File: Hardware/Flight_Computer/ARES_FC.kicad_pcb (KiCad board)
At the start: 2 copper layers, 57.2 x 57.2 mm, 63 parts, among them J1 SWD, J2 TYPE-C-31-M-12, J3 FC_M/P, J4 5V, J5 GND, J6 FC_RF, U1 STM32F401CCU6, U2 AMS1117-3.3, U3 BMP280, U4 BNO055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

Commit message: added tentative external i2c connectors
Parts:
- added J7: Conn_01x04_Pin, Connector_JST:JST_SH_BM04B-SRSS-TB_1x04-1MP_P1.00mm_Vertical, F.Cu at (147.2, 63.1)
- added J8: Conn_01x04_Pin, Connector_JST:JST_SH_BM04B-SRSS-TB_1x04-1MP_P1.00mm_Vertical, F.Cu at (161.3, 63.2)

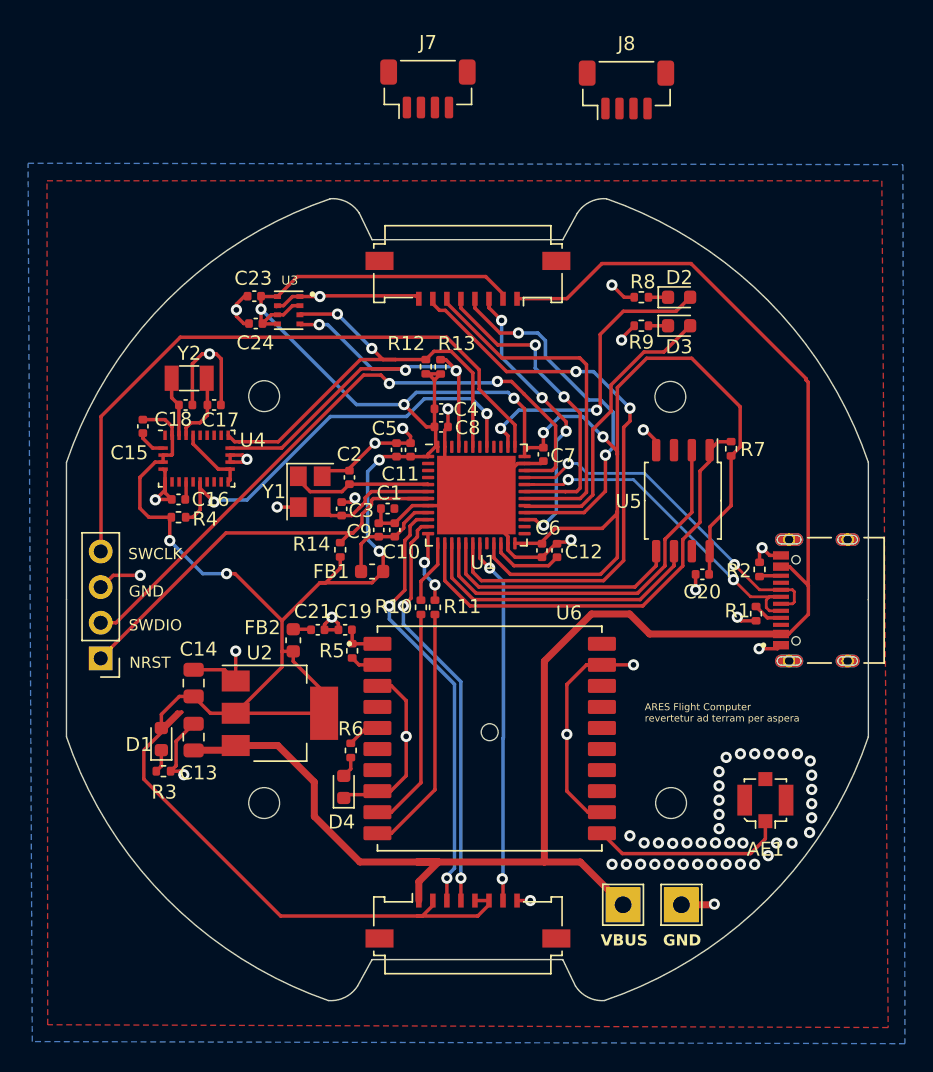
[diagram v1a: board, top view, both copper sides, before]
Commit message: fixed motor conn. i2c and external i2c conn.s, changed PNs, added models
new PN for Y2, added 3D models for BMP, Antenna, and ext. i2c connectors.
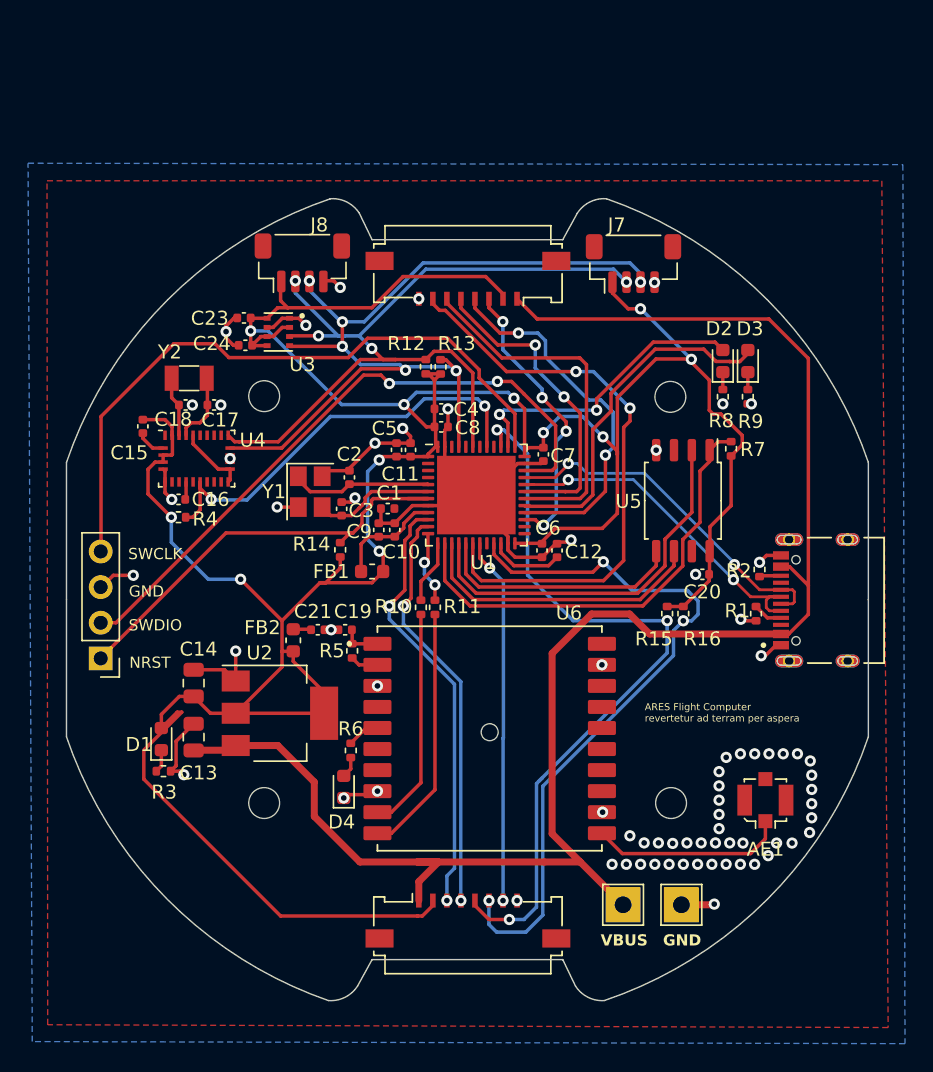
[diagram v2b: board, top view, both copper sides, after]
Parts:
- added R15: 4.7k, Resistor_SMD:R_0402_1005Metric, F.Cu at (164.2, 100.5)
- added R16: 4.7k, Resistor_SMD:R_0402_1005Metric, F.Cu at (165.3, 100.5)
- Y2: value 32.768Mhz -> 32.768kHz
- moved J8 26.2 mm to (138.2, 75.5)
- moved J7 19.2 mm to (161.8, 75.5)
- moved R8 9.16 mm to (168.2, 85.0), turned to -90 degrees
- moved R9 9.12 mm to (169.9, 85.0), turned to -90 degrees
- moved D2 5.52 mm to (168.2, 82.5), turned to 90 degrees
- moved D3 5.51 mm to (169.9, 82.5), turned to 90 degrees
- moved C23 1.72 mm to (134.0, 79.4)
- moved C24 1.72 mm to (134.1, 81.4)
- moved U3 1.72 mm to (136.5, 80.4)
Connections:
- J3 pad 5: +3.3V -> /MOTOR_SDA
- J3 pad 6: +3.3V -> /MOTOR_SCL
- U1 pad 21: +3.3V -> /MOTOR_SCL
- U1 pad 39: +3.3V -> /MOTOR_SDA
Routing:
- net GND: track 137.0 -> 82.3 mm, vias 67 -> 73
- net /MOTOR_SDA: track 0.00 -> 54.3 mm, vias 0 -> 3
- net /MOTOR_SCL: track 0.00 -> 51.0 mm, vias 0 -> 3
- net /SCL: track 34.6 -> 64.8 mm, vias 3 -> 6
- net /SDA: track 34.4 -> 62.0 mm, vias 2 -> 4
- net +3.3V: track 242.7 -> 236.1 mm, vias 9 -> 11
- net /LED_B: track 21.0 -> 25.0 mm
- net /SWCLK: track 46.4 -> 47.2 mm
- net /LED_G: track 21.9 -> 21.3 mm
- net VBUS: track 122.5 -> 122.0 mm

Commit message: added BOMs
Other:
- board text added: "TO MOTOR/POWER BOARD"
- board text added: "TO RF BOARD"
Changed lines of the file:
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@@
 			(outputformat 1)
 			(mirror no)
-			(drillshape 1)
+			(drillshape 0)
 			(scaleselection 1)
-			(outputdirectory "")
+			(outputdirectory "manufacturing/gbr/")
 		)
 	)
@@
 		)
 	)
+	(gr_text "TO RF BOARD"
+		(at 147.25 79.95 0)
+		(layer "F.SilkS")
+		(effects
+			(font
+				(size 0.5 0.5)
+				(thickness 0.1)
+				(bold yes)
+			)
+			(justify left bottom)
+		)
+	)
 	(gr_text "ARES Flight Computer\nrevertetur ad terram per aspera"
 		(at 162.6 108.25 0)
@@
 		)
 	)
+	(gr_text "TO MOTOR/POWER BOARD"
+		(at 145.25 119.8 0)
+		(layer "F.SilkS")
+		(effects
+			(font
+				(size 0.5 0.5)
+				(thickness 0.1)
+				(bold yes)
+			)
+			(justify left bottom)
+		)
+	)
 	(gr_text "SWDIO\n"
 		(at 127.72054 101.3256 0)
@@
 	)
 	(segment
-		(start 147.1625 93.79974)
-		(end 146.336656 93.79974)
+		(start 144.45 99)
+		(end 145.5 97.95)
 		(width 0.25)
 		(layer "F.Cu")
@@
 	)
 	(segment
-		(start 145.873 94.915084)
-		(end 145.5 95.288084)
+		(start 145.873 94.263396)
+		(end 146.336656 93.79974)
 		(width 0.25)
 		(layer "F.Cu")
@@
 	)
 	(segment
-		(start 146.336656 93.79974)
+		(start 145.873 94.915084)
 		(end 145.873 94.263396)
 		(width 0.25)
@@
 	)
 	(segment
-		(start 145.5 98.824695)
-		(end 144.399997 99.924698)
-		(width 0.25)
-		(layer "F.Cu")
-		(net 69)
-	)
-	(segment
-		(start 145.873 94.263396)
+		(start 145.5 95.288084)
 		(end 145.873 94.915084)
 		(width 0.25)
@@
 	)
 	(segment
-		(start 145.5 95.288084)
-		(end 145.5 98.824695)
+		(start 146.336656 93.79974)
+		(end 147.1625 93.79974)
 		(width 0.25)
 		(layer "F.Cu")
@@
 	)
 	(segment
-		(start 144.399997 99.924698)
-		(end 144.399997 99.95)
+		(start 145.5 97.95)
+		(end 145.5 95.288084)
 		(width 0.25)
 		(layer "F.Cu")
@@
 	)
 	(via
-		(at 144.399997 99.95)
+		(at 144.45 99)
 		(size 0.8)
 		(drill 0.4)
@@
 	)
 	(segment
-		(start 149.042281 105.528677)
-		(end 144.399997 100.886393)
+		(start 144.45 99)
+		(end 144.45 100.936396)
 		(width 0.25)
 		(layer "B.Cu")
@@
 	)
 	(segment
-		(start 149.042281 118.65066)
-		(end 149.042281 105.528677)
+		(start 149.042281 105.528677)
+		(end 149.042281 118.65066)
 		(width 0.25)
 		(layer "B.Cu")
@@
 	)
 	(segment
-		(start 148.5 119.192941)
-		(end 149.042281 118.65066)
+		(start 149.042281 118.65066)
+		(end 148.5 119.192941)
 		(width 0.25)
 		(layer "B.Cu")
@@
 	)
 	(segment
-		(start 144.399997 100.886393)
-		(end 144.399997 99.95)
+		(start 144.45 100.936396)
+		(end 149.042281 105.528677)
 		(width 0.25)
 		(layer "B.Cu")
@@
 	)
 	(segment
-		(start 148.5 120.95)
-		(end 148.5 119.192941)
+		(start 148.5 119.192941)
+		(end 148.5 120.95)
 		(width 0.25)
 		(layer "B.Cu")
@@
 	)
 	(segment
-		(start 145.95 99.4)
-		(end 145.4 99.95)
+		(start 146.4 95.02448)
+		(end 146.4 94.575)
 		(width 0.25)
 		(layer "F.Cu")
@@
 	)
 	(segment
-		(start 147.1625 94.29974)
-		(end 146.67526 94.29974)
+		(start 145.95 98.65)
+		(end 145.95 95.47448)
 		(width 0.25)
 		(layer "F.Cu")
@@
 	)
 	(segment
-		(start 145.95 95.47448)
-		(end 145.95 99.4)
+		(start 145.6 99)
+		(end 145.95 98.65)
 		(width 0.25)
 		(layer "F.Cu")
@@
 	)
 	(segment
-		(start 146.4 95.02448)
-		(end 145.95 95.47448)
+		(start 145.95 95.47448)
+		(end 146.4 95.02448)
 		(width 0.25)
 		(layer "F.Cu")
@@
 	)
 	(segment
-		(start 146.67526 94.29974)
-		(end 146.4 94.575)
+		(start 146.4 94.575)
+		(end 146.67526 94.29974)
 		(width 0.25)
 		(layer "F.Cu")
@@
 	)
 	(segment
-		(start 146.4 94.575)
-		(end 146.4 95.02448)
+		(start 146.67526 94.29974)
+		(end 147.1625 94.29974)
 		(width 0.25)
 		(layer "F.Cu")
@@
 	)
 	(via
-		(at 145.4 99.95)
+		(at 145.6 99)
 		(size 0.8)
 		(drill 0.4)
@@
 	(segment
 		(start 149.492281 120.942281)
-		(end 149.492281 105.342281)
+		(end 149.5 120.95)
 		(width 0.25)
 		(layer "B.Cu")
@@
 	)
 	(segment
-		(start 145.4 101.25)
-		(end 145.4 99.95)
+		(start 145.6 101.45)
+		(end 149.492281 105.342281)
 		(width 0.25)
 		(layer "B.Cu")
@@
 	)
 	(segment
-		(start 149.5 120.95)
+		(start 149.492281 105.342281)
 		(end 149.492281 120.942281)
 		(width 0.25)
@@
 	)
 	(segment
-		(start 149.492281 105.342281)
-		(end 145.4 101.25)
+		(start 145.6 99)
+		(end 145.6 101.45)
 		(width 0.25)
 		(layer "B.Cu")

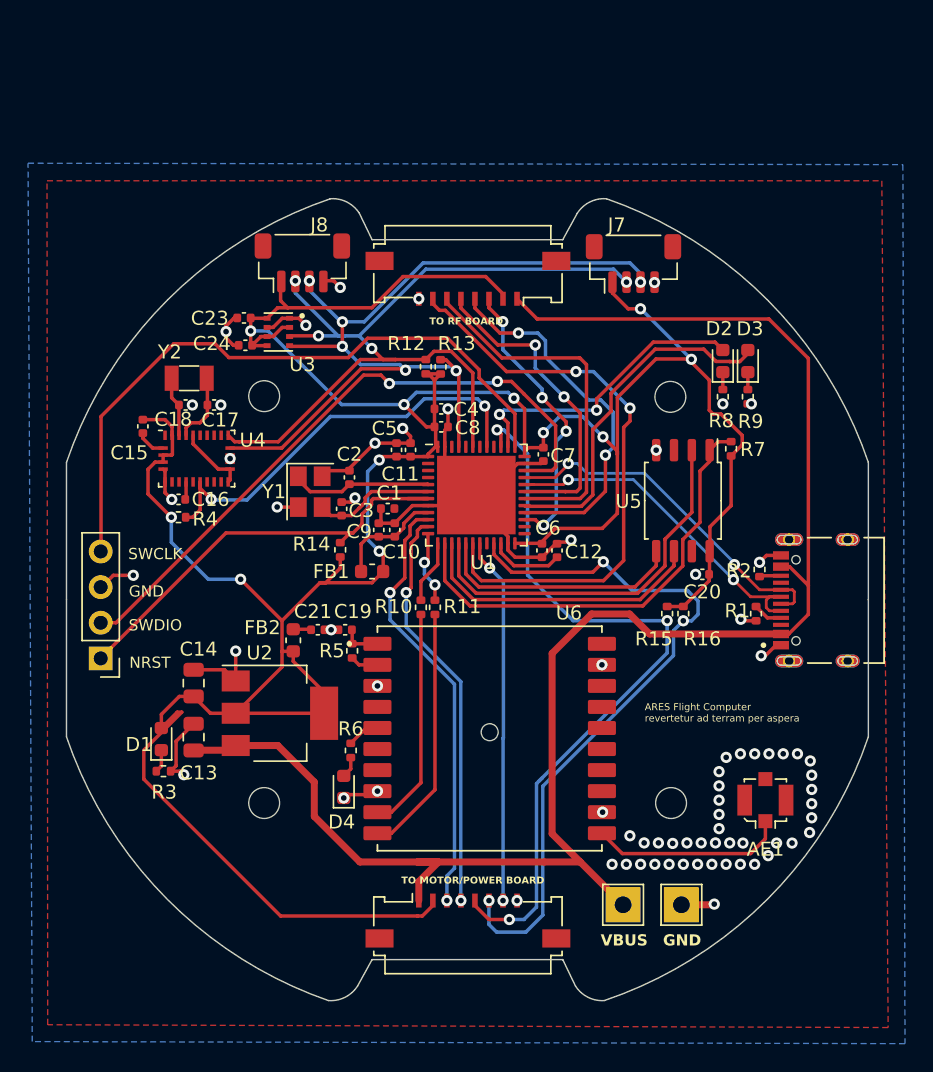
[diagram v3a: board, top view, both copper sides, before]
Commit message: Added Fencing Vias and ViPs to FC
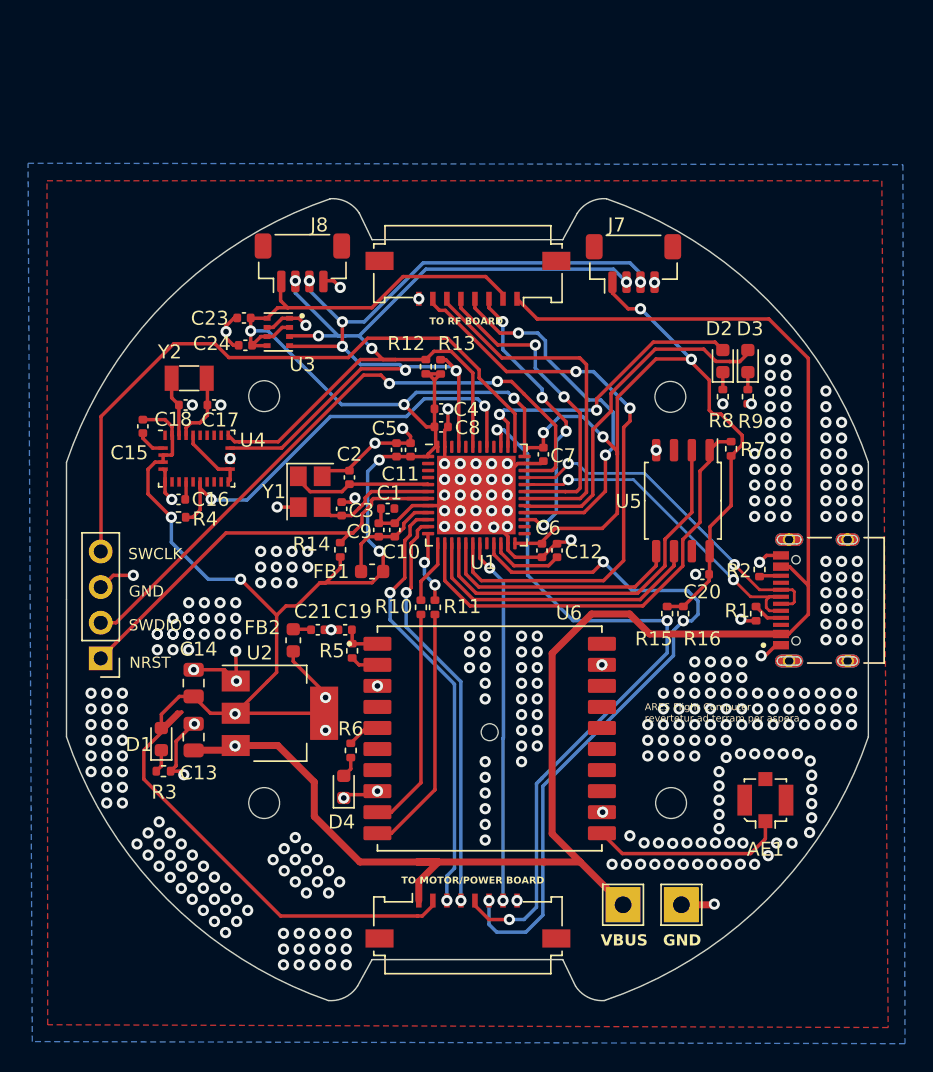
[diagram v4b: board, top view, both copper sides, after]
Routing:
- net +3.3V: track 236.1 -> 235.3 mm, vias 11 -> 14
- net GND: track 82.3 -> 82.4 mm, vias 73 -> 368
- net VBUS: vias 0 -> 1

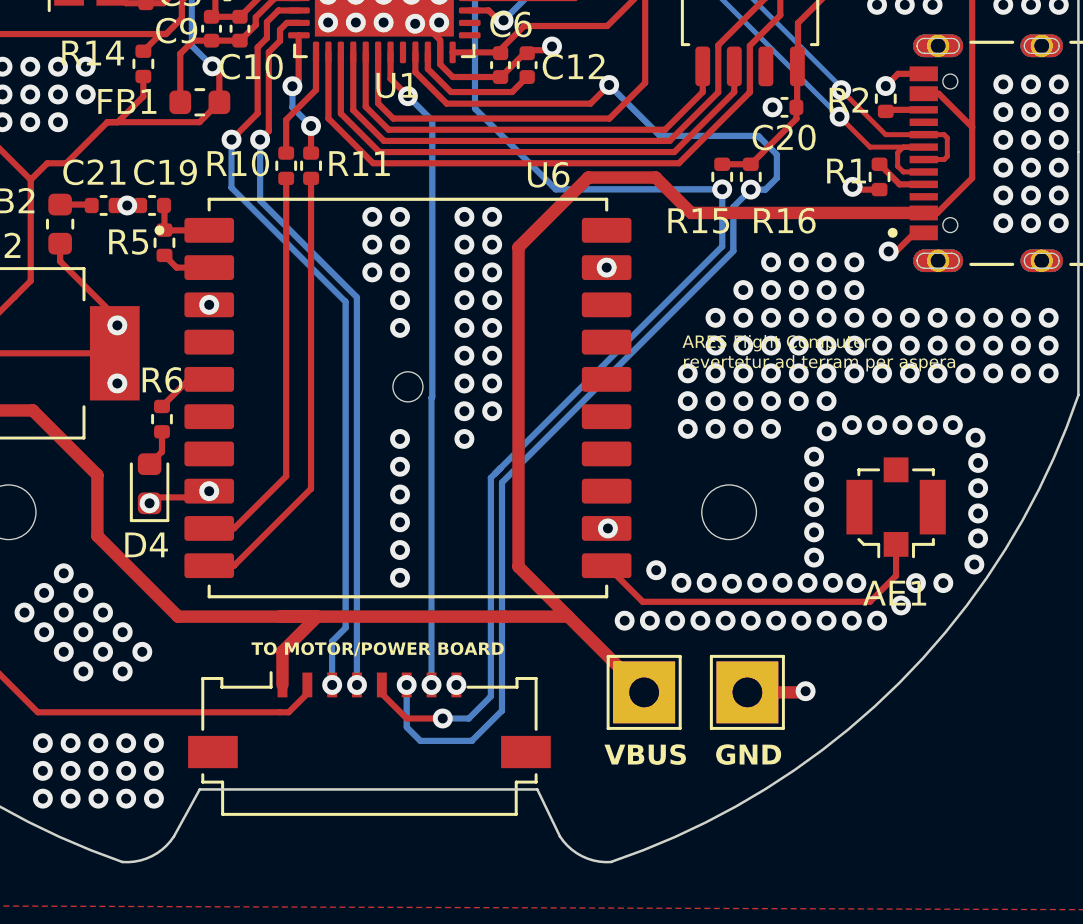
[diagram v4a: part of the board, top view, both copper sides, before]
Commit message: Removed front copper traced under GPS Increased GPS feed line width to be 50ohm Curved GPS feed line to reduce emmisions
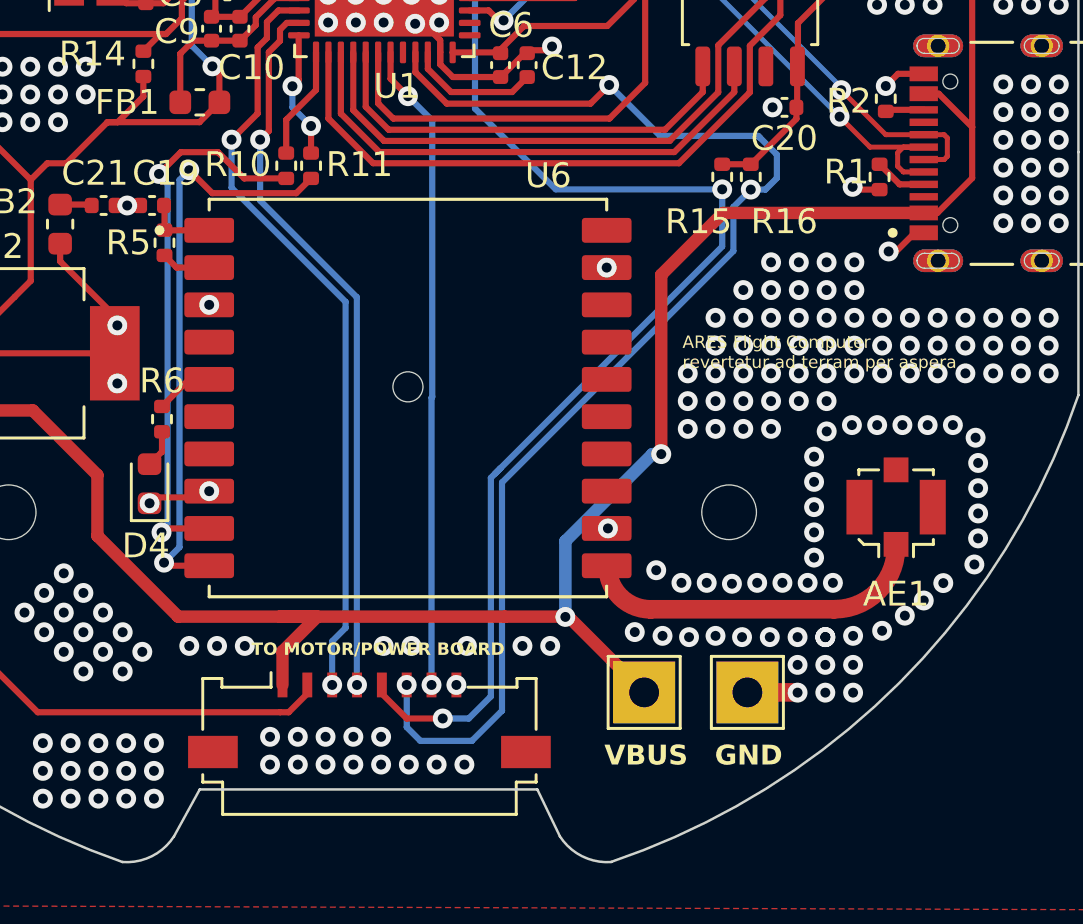
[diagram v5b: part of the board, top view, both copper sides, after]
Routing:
- net Net-(U6-TX): track 16.0 -> 22.7 mm, vias 0 -> 2
- net VBUS: track 122.0 -> 115.3 mm, vias 1 -> 3
- net Net-(AE1-A): track 13.9 -> 7.39 mm
- net Net-(U6-RX): track 17.9 -> 23.6 mm, vias 0 -> 2
- net GND: track 82.4 -> 82.1 mm, vias 368 -> 362
